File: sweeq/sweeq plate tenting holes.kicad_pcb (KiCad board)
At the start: 2 copper layers, 102 x 86.9 mm, 0 parts

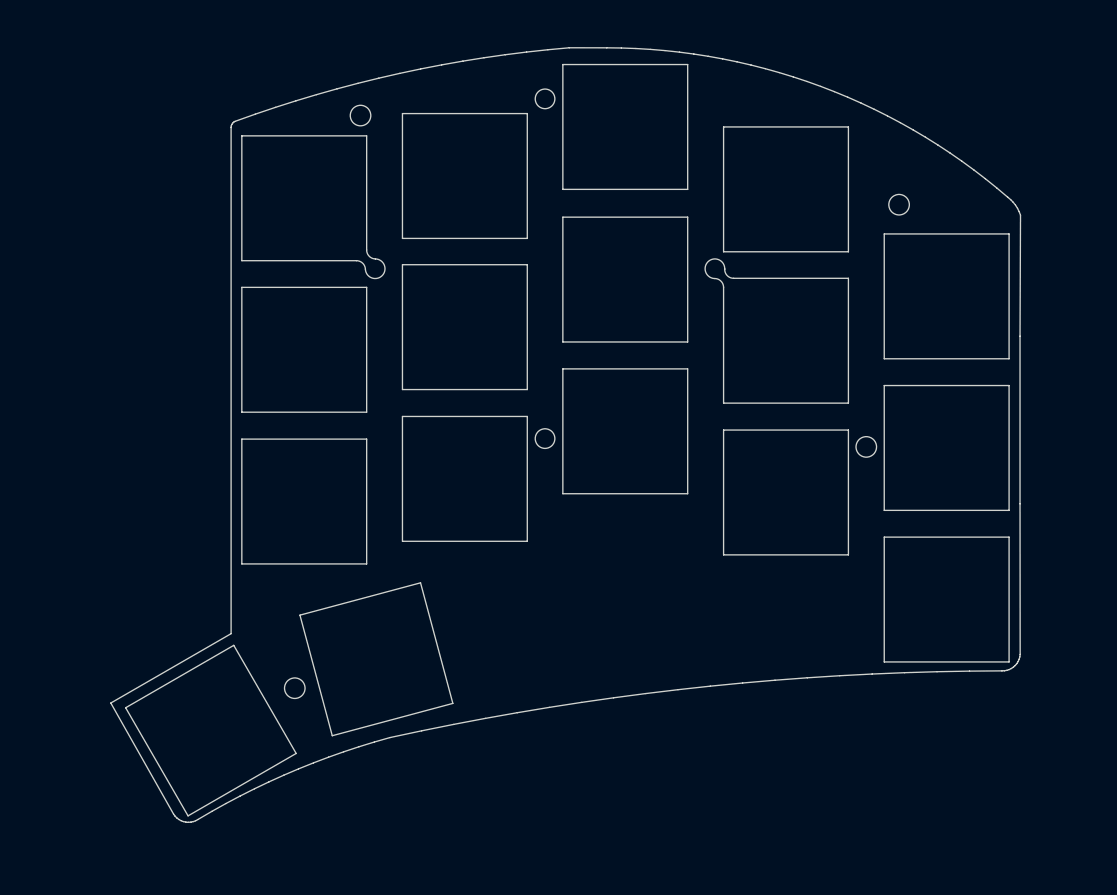
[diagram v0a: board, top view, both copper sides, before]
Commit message: sweeq: add the ferris graphics to the plate
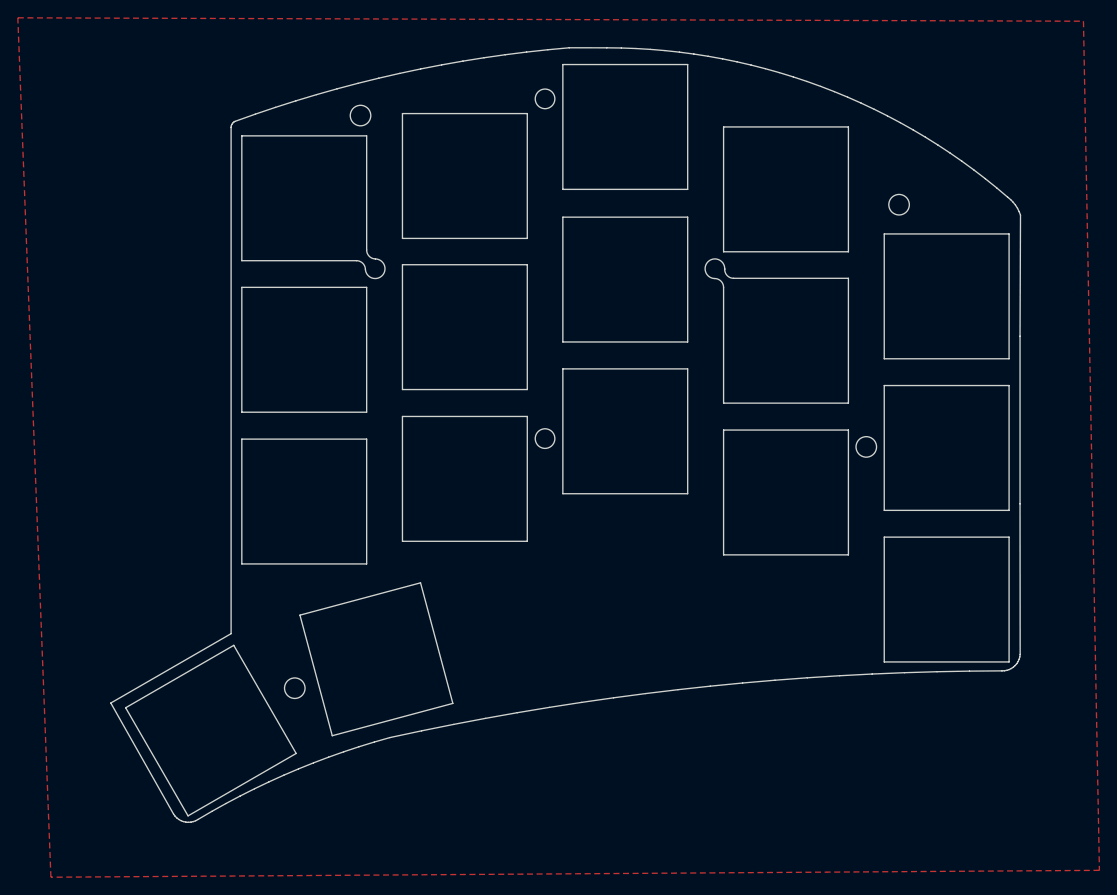
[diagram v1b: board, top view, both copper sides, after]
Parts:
- added G***: LOGO, holykeebs:footprint (4), F.Cu at (155.2, 114.0)
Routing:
- added copper zone on F.Cu, net (none)

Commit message: sweeq: fix left side tenting holes being 1mm off
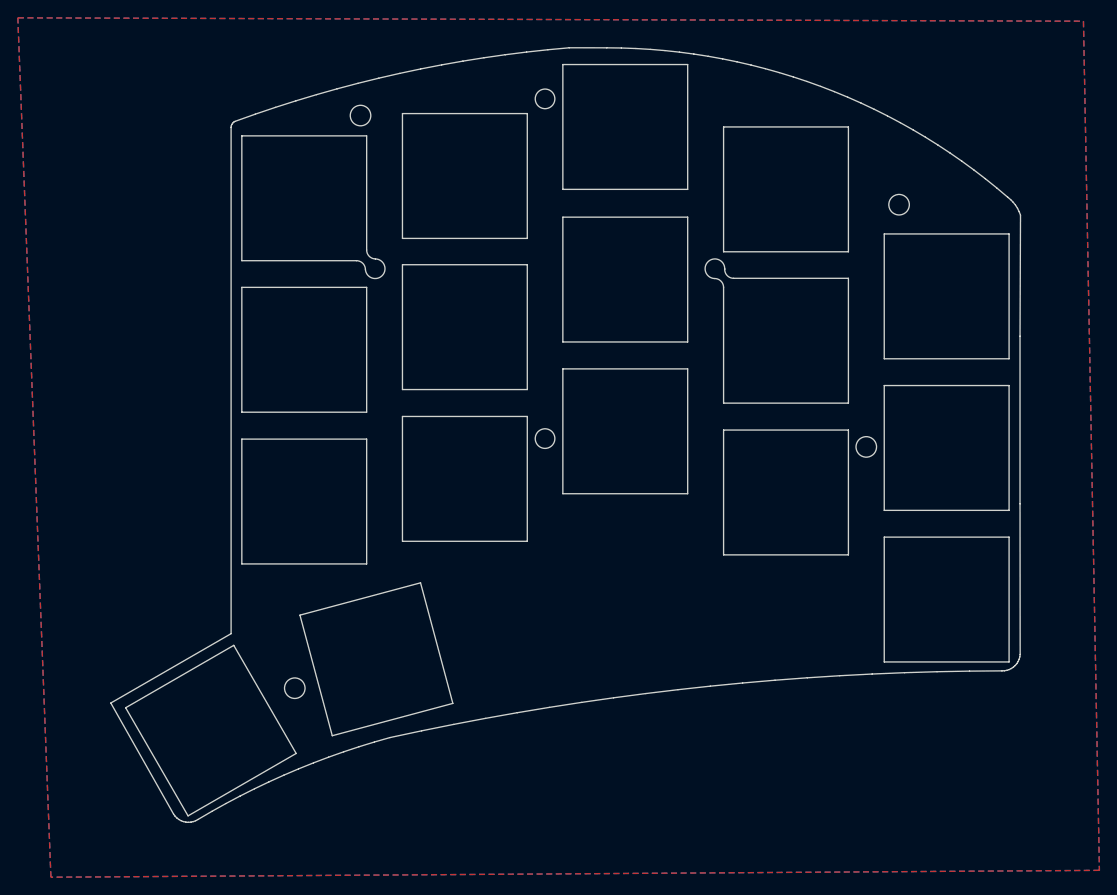
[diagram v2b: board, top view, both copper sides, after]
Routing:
- added copper zone on B.Cu, net (none)
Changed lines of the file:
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@@
   (gr_line (start 200.099945 69.004702) (end 199.95305 68.613622)
     (stroke (width 0.15) (type solid)) (layer "Edge.Cuts"))
-  (zone (net 0) (net_name "") (layer "F.Cu") (hatch edge 0.5)
+  (zone (net 0) (net_name "") (layers "F&B.Cu") (hatch edge 0.5)
     (connect_pads (clearance 0.5))
     (min_thickness 0.25) (filled_areas_thickness no)
